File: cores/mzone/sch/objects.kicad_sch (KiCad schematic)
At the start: 36 parts

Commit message: mzone core
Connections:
- net D'0: no longer C3.8 (D3)
- net D'1: no longer C3.7 (D2)
- net D'2: no longer C3.4 (D1)
- net D'3: now also C3.2 (Q0); no longer C3.3 (D0)
- net D'4: no longer C3.14 (D5)
- net D'5: no longer C3.17 (D6)
- net D'6: no longer C3.18 (D7)
- net D'7: no longer C3.13 (D4)
- net OCHA10: no longer C3.15 (Q5)
- net OCHA11: no longer C3.16 (Q6)
- net OCHA12: no longer C3.19 (Q7)
- net OCHA6: no longer C3.9 (Q3)
- net OCHA7: no longer C3.6 (Q2)
- net OCHA8: no longer C3.5 (Q1)
- net OCHA9: no longer C3.2 (Q0)
- net VCC: now also C3.3 (D0); no longer C3.1 (~{Mr})
- net ~{OCHAL}: no longer C3.12 (Q4)
- net ~{ODB}3: no longer C3.11 (Cp)
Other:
- moved on the sheet: C3

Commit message: mzone core
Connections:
- net D'0: now also C3.8 (D3)
- net D'1: now also C3.7 (D2)
- net D'2: now also C3.4 (D1)
- net D'3: now also C3.3 (D0); no longer C3.2 (Q0)
- net D'4: now also C3.14 (D5)
- net D'5: now also C3.17 (D6)
- net D'6: now also C3.18 (D7)
- net D'7: now also C3.13 (D4)
- net OCHA10: now also C3.15 (Q5)
- net OCHA11: now also C3.16 (Q6)
- net OCHA12: now also C3.19 (Q7)
- net OCHA6: now also C3.9 (Q3)
- net OCHA7: now also C3.6 (Q2)
- net OCHA8: now also C3.5 (Q1)
- net OCHA9: now also C3.2 (Q0)
- net VCC: now also C3.1 (~{Mr}); no longer C3.3 (D0)
- net ~{OCHAL}: now also C3.12 (Q4)
- net ~{ODB}3: now also C3.11 (Cp)
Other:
- moved on the sheet: C3

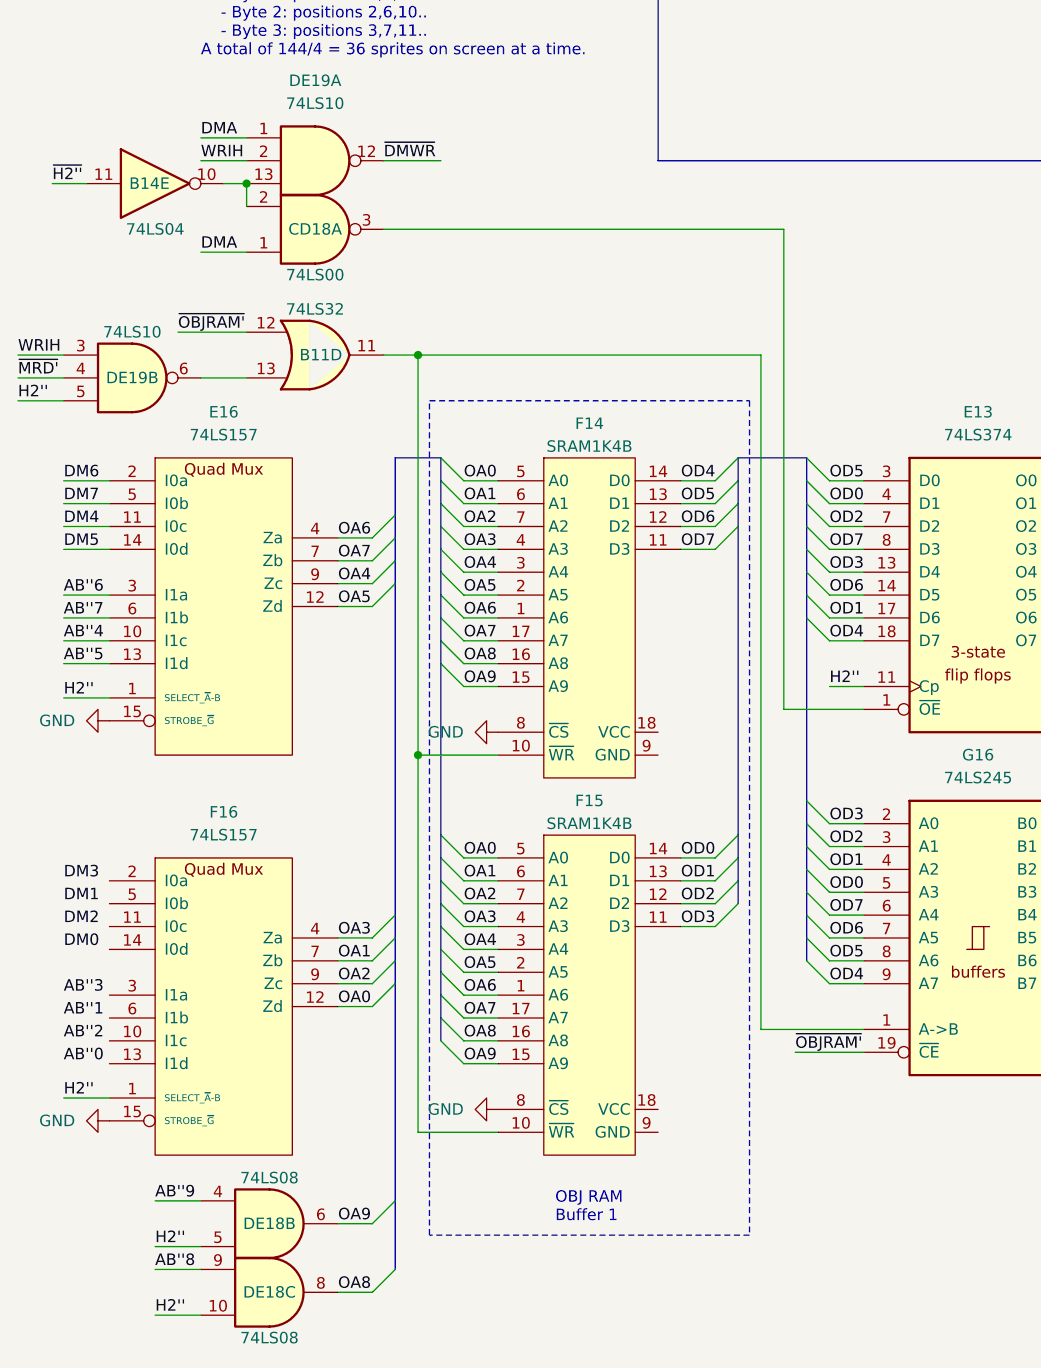
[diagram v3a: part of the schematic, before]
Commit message: mzone core
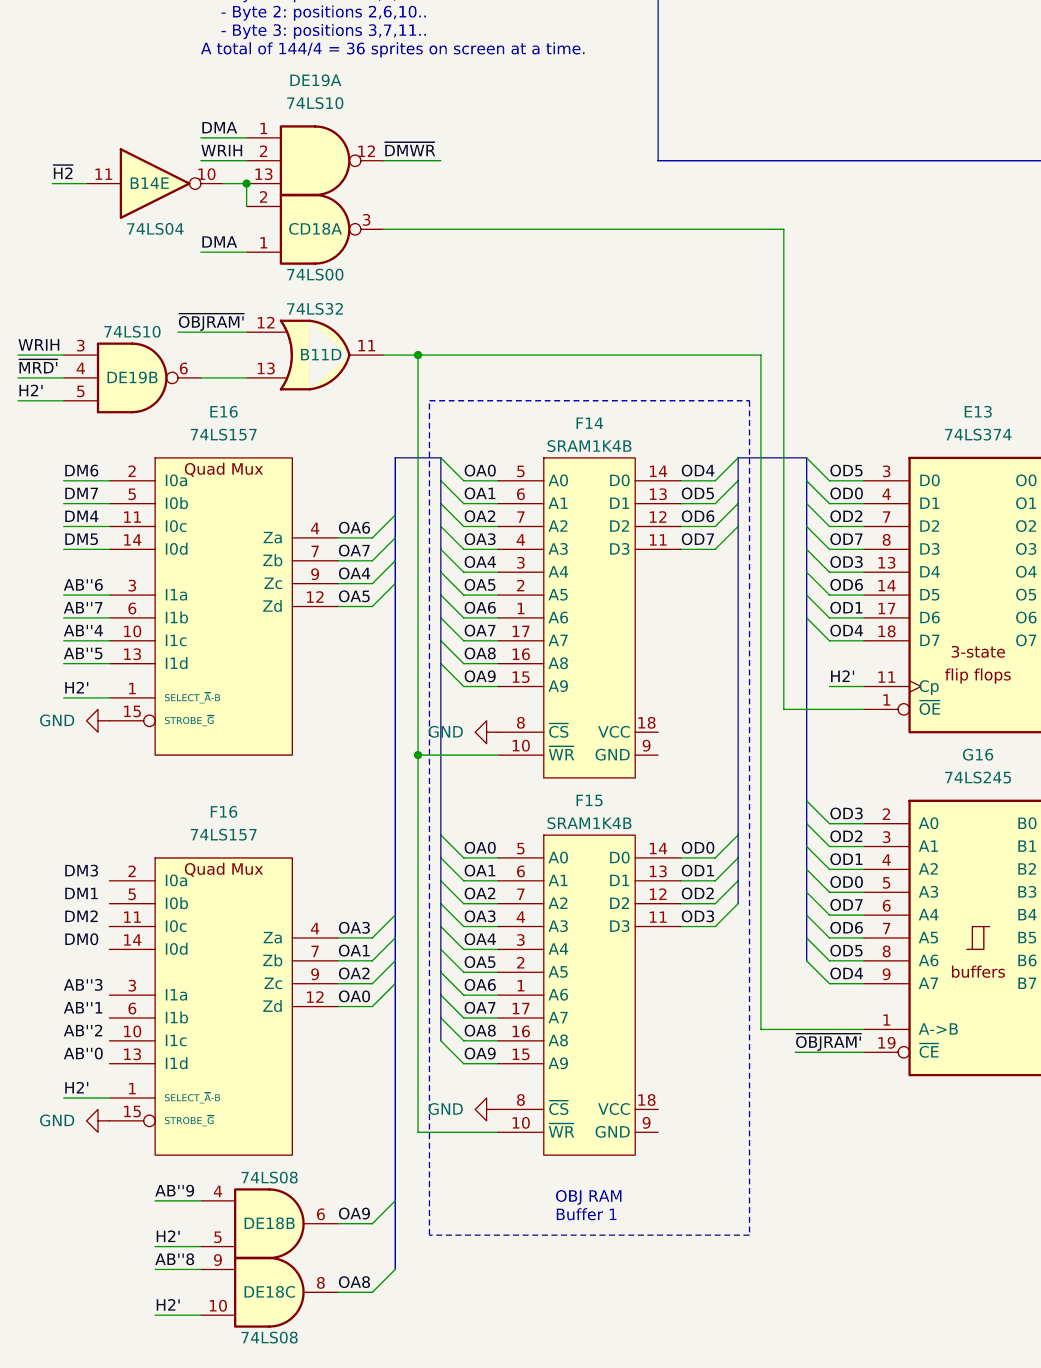
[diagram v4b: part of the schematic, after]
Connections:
- net H2'' renamed H2'
- net ~{H2''} renamed ~{H2}
